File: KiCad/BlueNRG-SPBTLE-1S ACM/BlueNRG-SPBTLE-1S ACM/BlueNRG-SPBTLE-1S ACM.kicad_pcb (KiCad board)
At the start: 2 copper layers, 25 x 30.5 mm, 12 parts, among them J1 Conn_01x04_Female, U1 LSM6DS3, U2 SPBTLE-1S

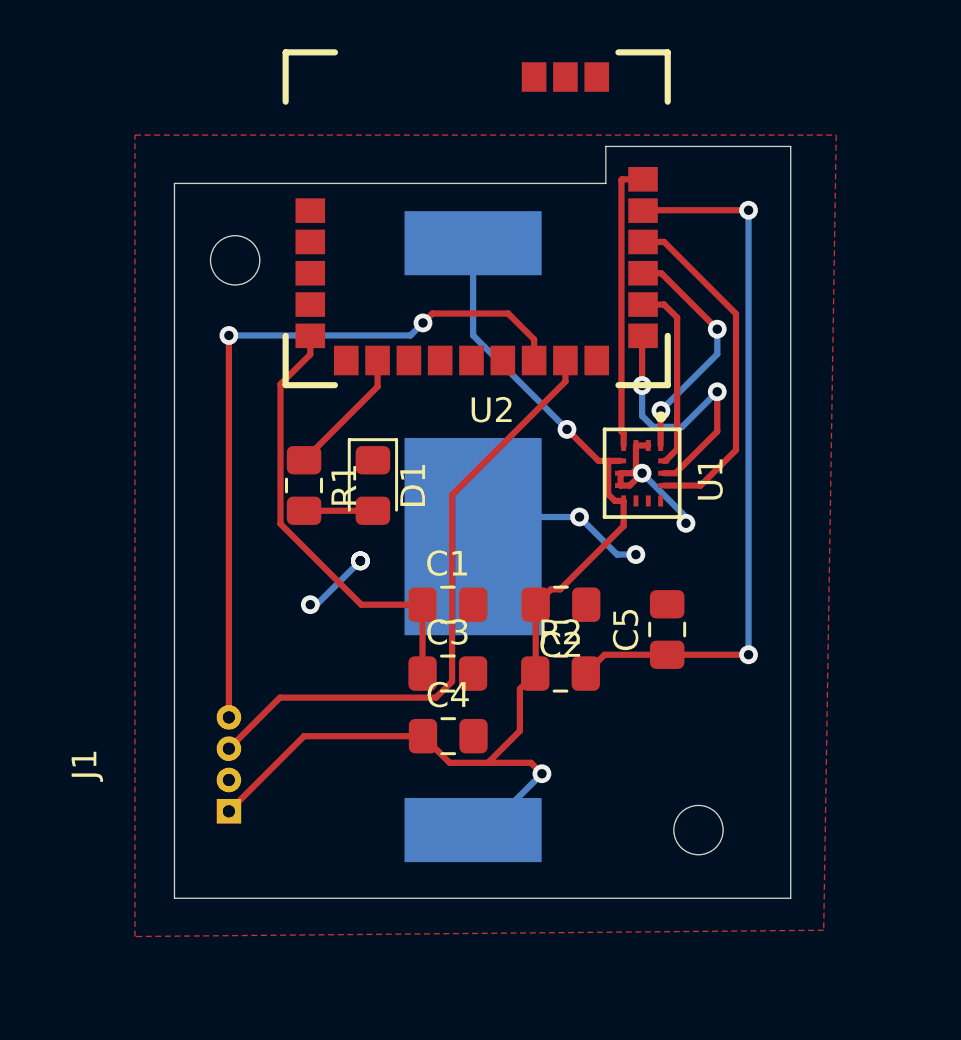
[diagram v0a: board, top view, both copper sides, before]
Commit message: Added a push button for the RST pin and an IC for the power management
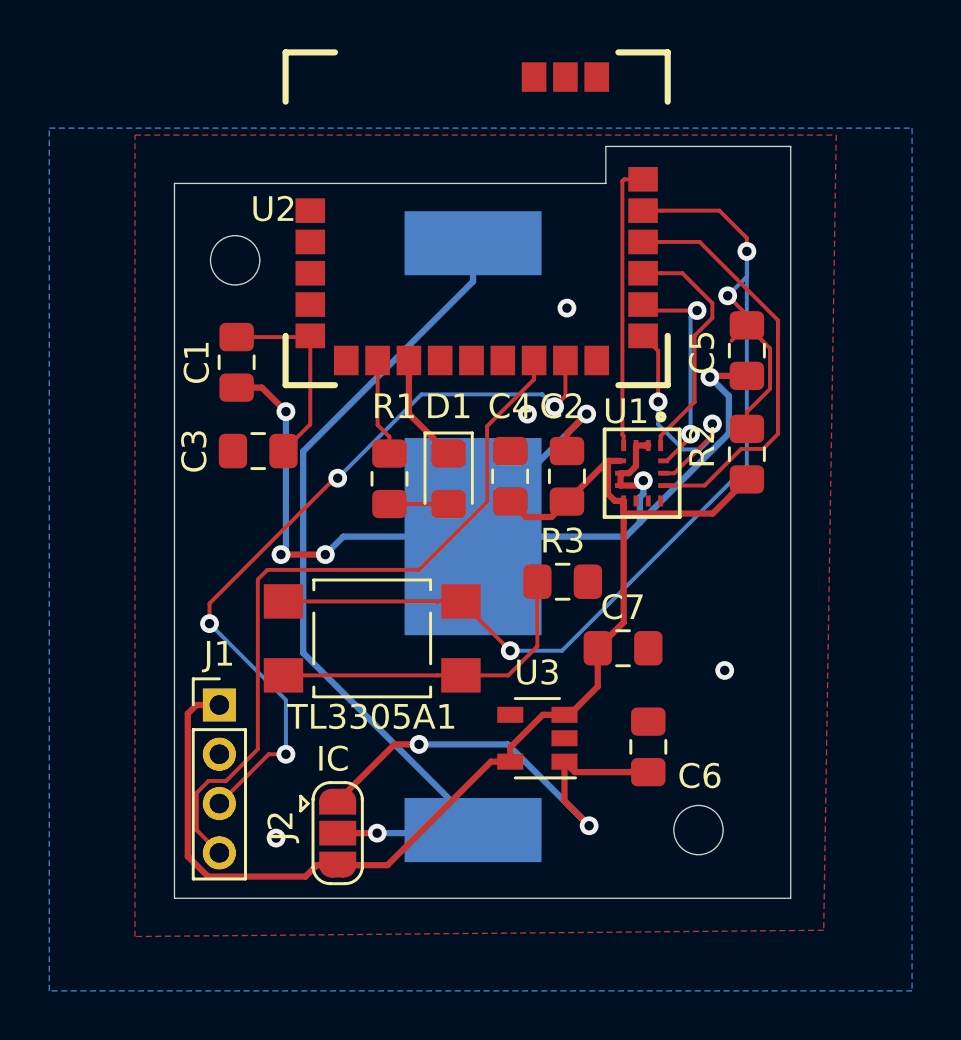
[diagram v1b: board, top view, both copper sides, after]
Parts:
- added C6: 1u, Capacitor_SMD:C_0805_2012Metric_Pad1.15x1.40mm_HandSolder, F.Cu at (157.2, 90.9)
- added C7: 1u, Capacitor_SMD:C_0805_2012Metric_Pad1.15x1.40mm_HandSolder, F.Cu at (156.2, 86.9)
- added J2: Conn_01x03, Jumper:SolderJumper-3_P1.3mm_Open_RoundedPad1.0x1.5mm, F.Cu at (144.6, 94.4)
- added R3: 100k, Resistor_SMD:R_0805_2012Metric_Pad1.15x1.40mm_HandSolder, F.Cu at (153.7, 84.2)
- added TL3305A1: SW_Push_Dual, Button_Switch_SMD:SW_SPST_TL3305A, F.Cu at (146.0, 86.5)
- added U3: TLV70033_SOT23-5, Package_TO_SOT_SMD:SOT-23-5, F.Cu at (152.7, 90.5)
- J1: footprint SPBTLE-1S:JTAG-SWD-4PINS -> Socket_Strips:Socket_Strip_Straight_1x04_Pitch2.00mm
- R2: value 47k -> 100k
- moved C1 13.0 mm to (140.5, 75.3), turned to 270 degrees
- moved C3 11.9 mm to (141.4, 78.9), turned to 180 degrees
- moved C5 11.8 mm to (161.2, 74.8), turned to 270 degrees
- moved R2 11.7 mm to (161.2, 79.0), turned to 90 degrees
- moved C4 10.8 mm to (151.6, 79.9), turned to 90 degrees
- moved C2 5.21 mm to (153.9, 79.9), turned to 270 degrees
- moved R1 3.48 mm to (146.7, 80.0)
- moved D1 3.08 mm to (149.1, 80.0)
- moved J1 2.44 mm to (139.8, 89.2), turned to 0 degrees
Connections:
- BT1 pad 1: Vdd -> Net-(BT1-Pad1)
- J1 pad 1: JTCK-SWCTK -> Vdd
- J1 pad 2: JTMS-SWTDIO -> GND
- J1 pad 3: GND -> JTMS-SWTDIO
- J1 pad 4: Vdd -> JTCK-SWCTK
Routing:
- net Net-(BT1-Pad1): track 0.00 -> 35.1 mm, vias 0 -> 1
- net GND: track 16.8 -> 51.1 mm, vias 8 -> 10
- net Net-(C6-Pad2): track 0.00 -> 19.1 mm, vias 0 -> 2
- net Net-(C5-Pad1): track 29.2 -> 46.2 mm, vias 2 -> 3
- net Net-(R3-Pad1): track 0.00 -> 13.4 mm
- net Net-(C1-Pad1): track 18.0 -> 8.13 mm
- net JTMS-SWTDIO: track 25.1 -> 30.7 mm, vias 0 -> 4
- net Vdd: track 45.4 -> 49.5 mm, vias 2 -> 0
- net SPI_CS: track 14.0 -> 17.3 mm
- net SPI_OUT: track 7.68 -> 9.02 mm, vias 0 -> 2
- net Net-(R1-Pad1): track 5.28 -> 3.97 mm
- net SPI_CLK: track 11.6 -> 10.3 mm
- net JTCK-SWCTK: track 29.5 -> 30.0 mm, vias 2 -> 0
- net SPI_IN: track 9.62 -> 10.1 mm, vias 2 -> 0
- added copper zone on B.Cu, net GND
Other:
- net class Default: clearance 0.15 -> 0.16
- rule trace_clearance: 0.15 -> 0.16
- rule trace_min: 0.1524 -> 0.16
- board text added: "GND"
- board text added: "IC"
